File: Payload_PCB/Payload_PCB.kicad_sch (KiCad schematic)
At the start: 22 parts, among them J2 Conn_01x03, J3 Conn_01x03, J4 Conn_01x03, Q4 PMOS, Q5 PMOS, Q6 NMOS, U1 TSR_1-2450

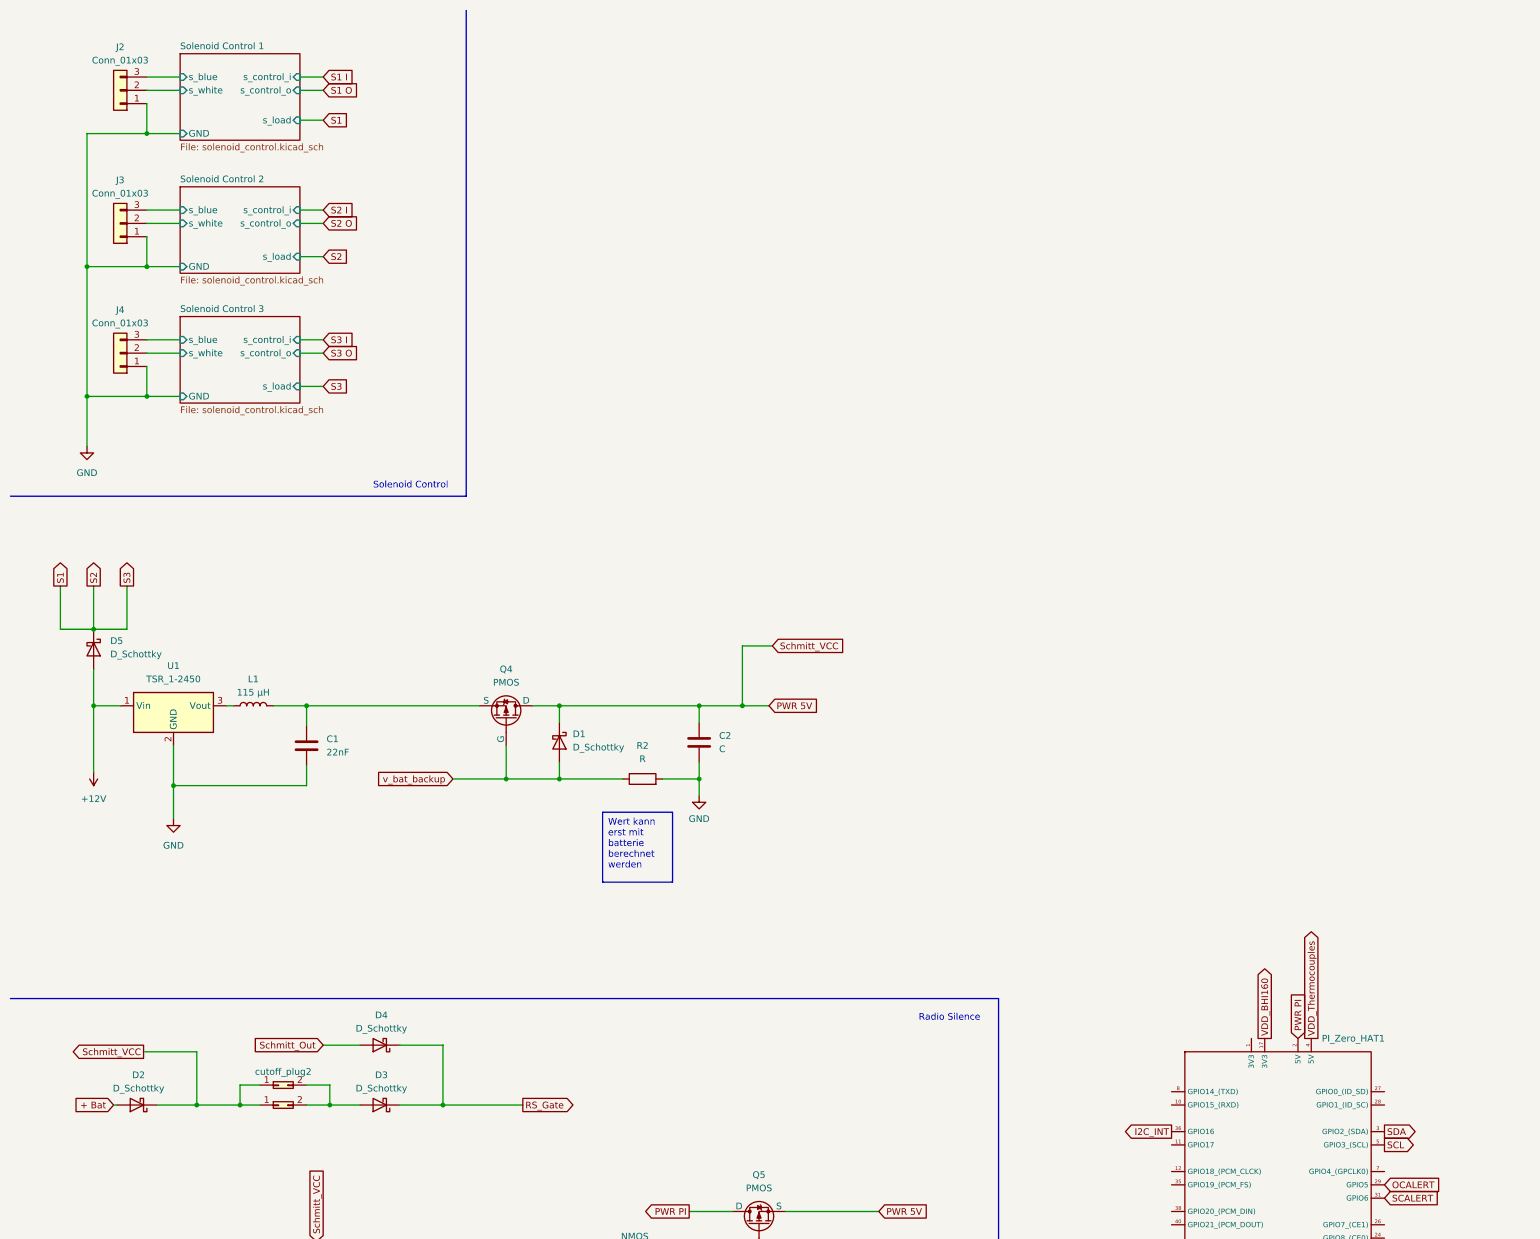
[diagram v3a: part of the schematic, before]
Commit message: Added bms chip (not yet connected to power)
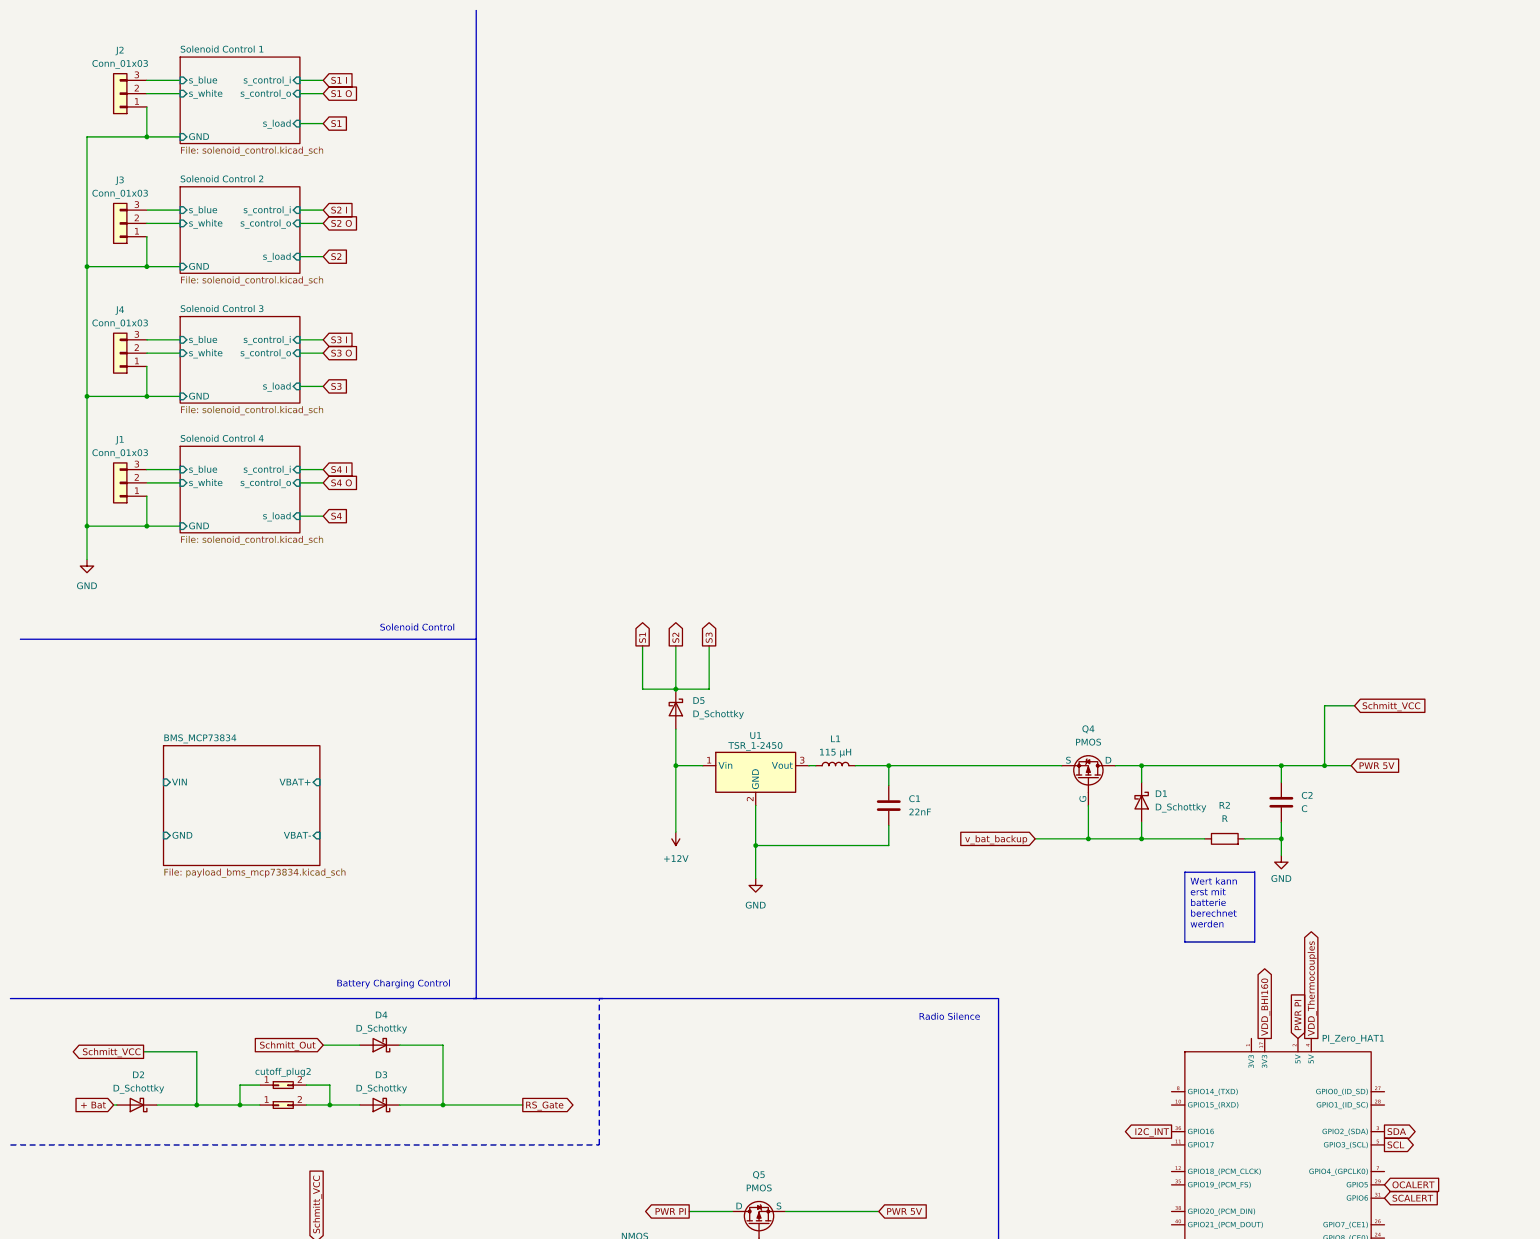
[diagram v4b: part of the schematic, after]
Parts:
- added J1: Conn_01x03, symbol Connector_Generic:Conn_01x03
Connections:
- net GND: now also J1.1 (Pin_1)
- new net Solenoid Control 4/s_blue: J1.3 (Pin_3)
- new net Solenoid Control 4/s_white: J1.2 (Pin_2)
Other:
- added sheet BMS_MCP73834 (payload_bms_mcp73834.kicad_sch)
- added sheet Solenoid Control 4 (solenoid_control.kicad_sch)
- note added: "Battery Charging Control"
- moved on the sheet: C1, C2, D1, D5, J2, L1, Q4, R2, U1

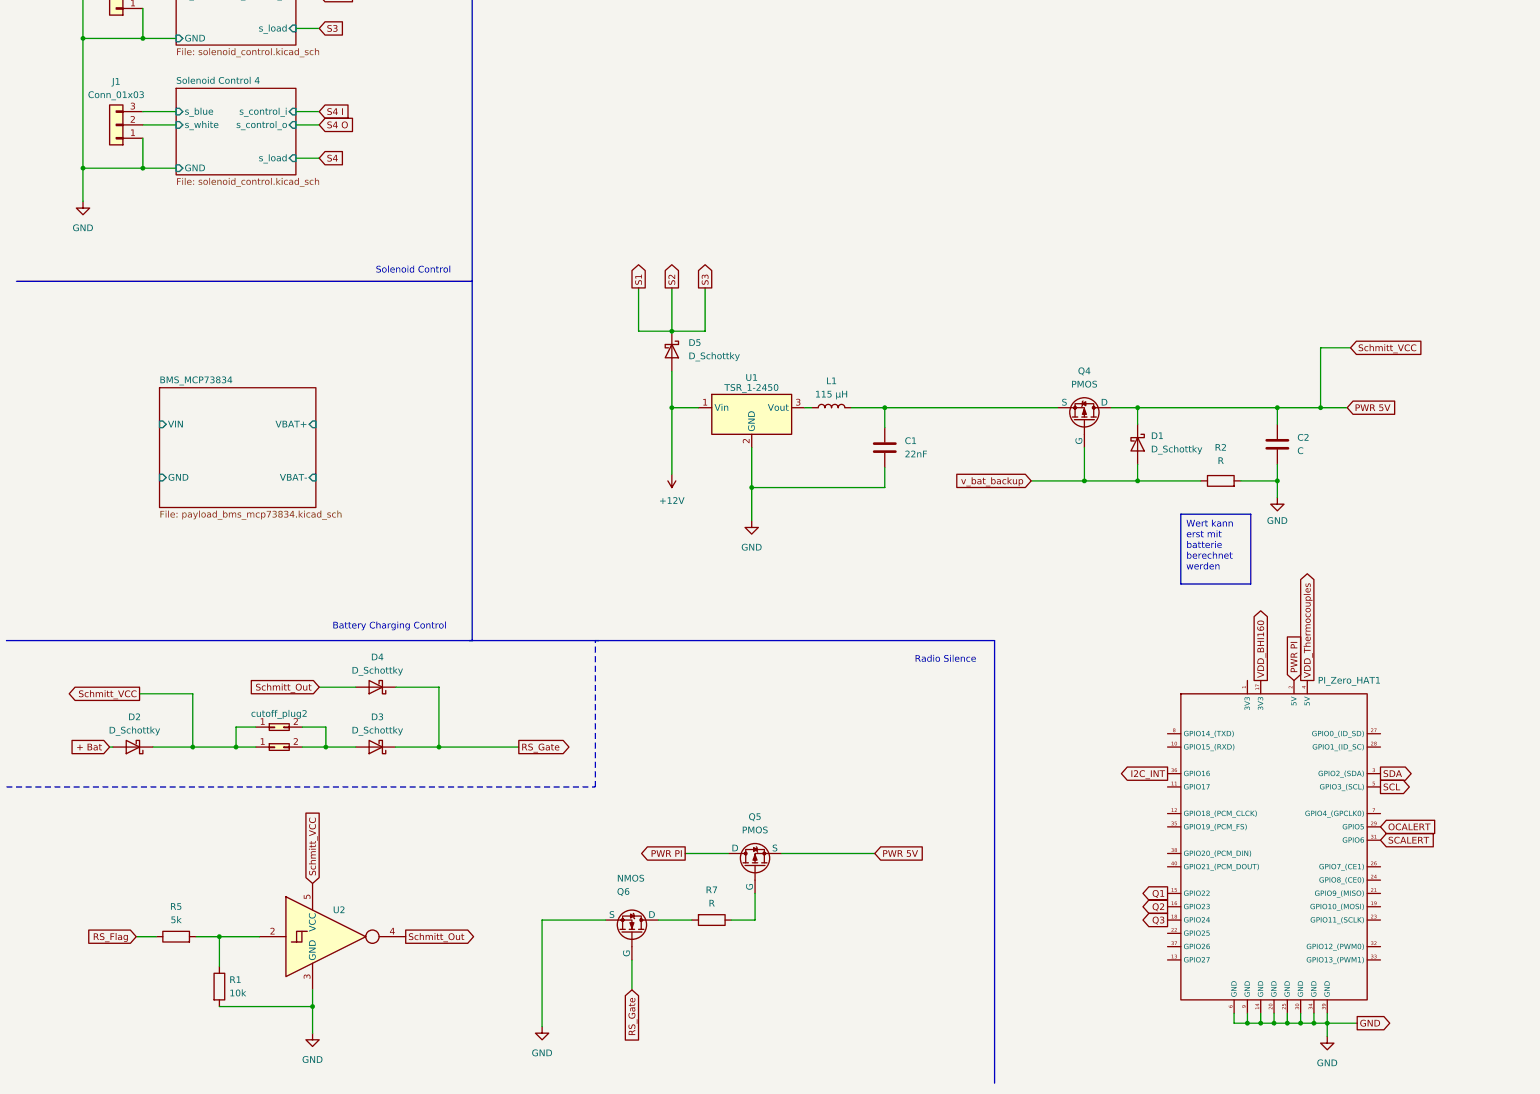
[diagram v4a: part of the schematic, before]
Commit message: Added Payload Harness Connector
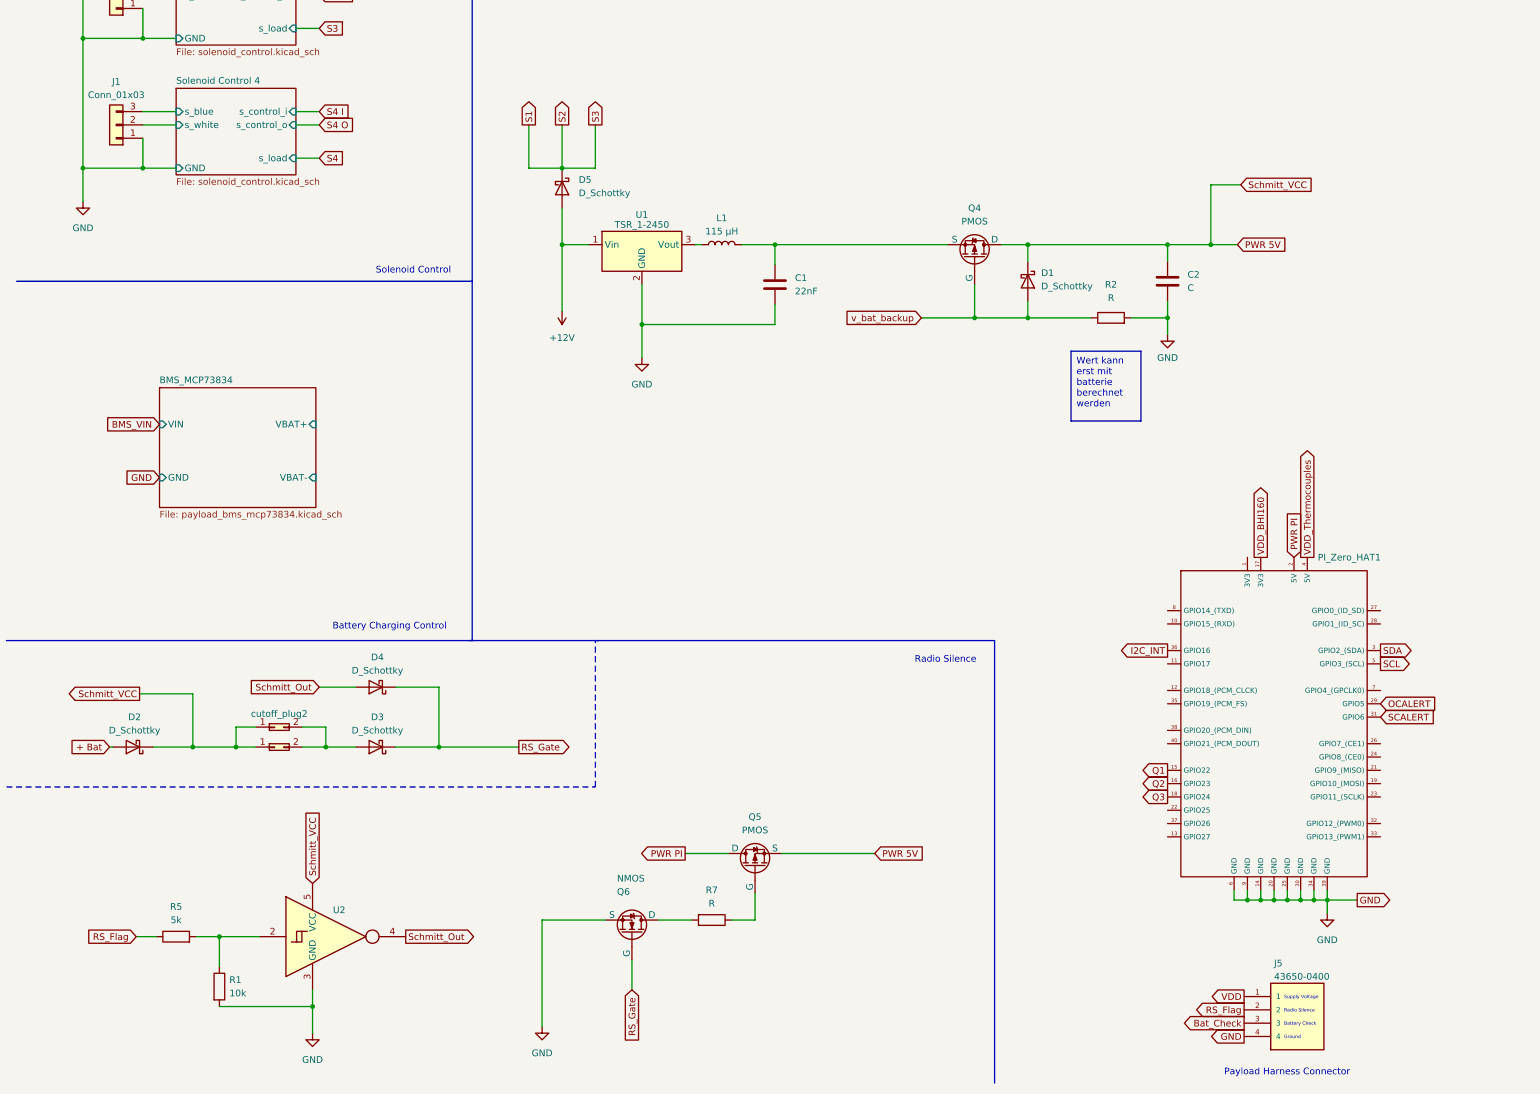
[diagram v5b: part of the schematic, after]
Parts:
- added J5: 43650-0400, 43650-0400:MOLEX_43650-0400, symbol 43650-0400:43650-0400
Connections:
- net GND: now also J5.4
- net RS_Flag: now also J5.2
- new net Bat_Check: J5.3
- new net VDD: J5.1
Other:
- note added: "Battery Check"
- note added: "Ground"
- note added: "Payload Harness Connector"
- note added: "Supply Voltage"
- moved on the sheet: C1, C2, D1, D5, L1, PI_Zero_HAT1, Q4, R2, U1

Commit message: Minor changes and corrections
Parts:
- added C18: 22nF, symbol Device:C
- added L2: 115 µH, symbol Device:L
- added U10: TSR_1-2450, Converter_DCDC:Converter_DCDC_TRACO_TSR-1_THT, symbol Regulator_Switching:TSR_1-2450
- renumbered D2 to D1, D4 to D2, D5 to D4, D1 to D5, J2 to J1, J3 to J2, J4 to J3, J1 to J4, Q6 to Q1, Q5 to Q2, Q4 to Q3, R5 to R1, R1 to R2, R7 to R3, R2 to R4, U2 to U1, U1 to U2, cutoff_plug2 to cutoff_plug1
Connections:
- net Q1 is gone; now on net S1 I: PI_Zero_HAT1.15 (GPIO22)
- net Q2 is gone; now on net S1 O: PI_Zero_HAT1.16 (GPIO23)
- net Q3 is gone; now on net S2 I: PI_Zero_HAT1.18 (GPIO24)
- net GND: now also C18.2, U10.2 (GND)
- net I2C_INT: now also PI_Zero_HAT1.8 (GPIO14_(TXD)); no longer PI_Zero_HAT1.36 (GPIO16)
- net S2 O: now also PI_Zero_HAT1.22 (GPIO25)
- net S3 I: now also PI_Zero_HAT1.37 (GPIO26)
- net S3 O: now also PI_Zero_HAT1.13 (GPIO27)
- net S4 I: now also PI_Zero_HAT1.36 (GPIO16)
- net S4 O: now also PI_Zero_HAT1.11 (GPIO17)
- net +12V renamed S_LOAD
- net S_LOAD: no longer U2.1 (Vin)
- net v_bat_backup: no longer names the net of D5.2 (A), Q3.2 (G), R4.1
- net v_bat_backup: now also C18.1, L2.2
- new net: L2.1, U10.3 (Vout)
- new net VBAT+: U2.1 (Vin)
- new net VBAT+_Backup: U10.1 (Vin)
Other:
- added sheet BMS_MCP73835 (payload_bms_mcp73834.kicad_sch)
- sheet BMS_MCP73834 ports: added none; removed VBAT-
- moved on the sheet: C1, D4, L1, U2

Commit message: Added BMI088 and BMP390
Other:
- note added: "backup_bat"
- note added: "main_bat"
- note added: "Änderung zu boost convertern nötig"
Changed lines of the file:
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@@
     (effects (font (size 1.27 1.27)) (justify left top))
+  )
+  (text "Änderung zu boost convertern nötig\n" (at 125.73 113.665 0)
+    (effects (font (size 1.27 1.27)) (justify left bottom))
   )
   (text "TODO: Maybe only one VDD and distribute among sensors?\n"
@@
     (effects (font (size 0.635 0.635)) (justify left bottom))
   )
+  (text "backup_bat\n" (at 43.815 165.1 0)
+    (effects (font (size 1.27 1.27)) (justify left bottom))
+  )
   (text "Radio Silence" (at 255.905 271.78 0)
     (effects (font (size 0.635 0.635)) (justify left bottom))
   )
-  (text "Battery Charging Control\n" (at 74.295 198.755 0)
+  (text "Battery Charging Control\n" (at 80.645 198.755 0)
     (effects (font (size 1.27 1.27)) (justify left bottom))
   )
@@
     (effects (font (size 1.27 1.27)) (justify left bottom))
   )
+  (text "main_bat" (at 43.815 137.795 0)
+    (effects (font (size 1.27 1.27)) (justify left bottom))
+  )
   (text "Solenoid Control" (at 82.55 130.81 0)
     (effects (font (size 1.27 1.27)) (justify left bottom))
@@
     )
   )
-  (global_label "GND" (shape input) (at 44.45 182.88 180) (fields_autoplaced)
-    (effects (font (size 1.27 1.27)) (justify right))
-    (property "Intersheetrefs" "${INTERSHEET_REFS}" (at 37.5943 182.88 0)
+  (global_label "GND" (shape input) (at 43.815 182.88 180) (fields_autoplaced)
+    (effects (font (size 1.27 1.27)) (justify right))
+    (property "Intersheetrefs" "${INTERSHEET_REFS}" (at 36.9593 182.88 0)
       (effects (font (size 1.27 1.27)) (justify right) hide)
     )
@@
     )
   )
-  (global_label "VBAT+_Backup" (shape output) (at 61.595 177.165 0) (fields_autoplaced)
-    (effects (font (size 1.27 1.27)) (justify left))
-    (property "Intersheetrefs" "${INTERSHEET_REFS}" (at 78.3687 177.165 0)
+  (global_label "VBAT+_Backup" (shape output) (at 60.96 177.165 0) (fields_autoplaced)
+    (effects (font (size 1.27 1.27)) (justify left))
+    (property "Intersheetrefs" "${INTERSHEET_REFS}" (at 77.7337 177.165 0)
       (effects (font (size 1.27 1.27)) (justify left) hide)
     )
@@
     )
   )
-  (global_label "BMS_VIN" (shape input) (at 44.45 172.72 180) (fields_autoplaced)
-    (effects (font (size 1.27 1.27)) (justify right))
-    (property "Intersheetrefs" "${INTERSHEET_REFS}" (at 33.5424 172.72 0)
+  (global_label "BMS_VIN" (shape input) (at 43.815 172.72 180) (fields_autoplaced)
+    (effects (font (size 1.27 1.27)) (justify right))
+    (property "Intersheetrefs" "${INTERSHEET_REFS}" (at 32.9074 172.72 0)
       (effects (font (size 1.27 1.27)) (justify right) hide)
     )
@@
     )
   )
-  (sheet (at 44.45 168.275) (size 17.145 17.78) (fields_autoplaced)
+  (sheet (at 43.815 168.275) (size 17.145 17.78) (fields_autoplaced)
     (stroke (width 0.1524) (type solid))
     (fill (color 0 0 0 0.0000))
-    (property "Sheetname" "BMS_MCP73835" (at 44.45 167.5634 0)
+    (property "Sheetname" "BMS_MCP73835" (at 43.815 167.5634 0)
       (effects (font (size 1.27 1.27)) (justify left bottom))
     )
-    (property "Sheetfile" "payload_bms_mcp73834.kicad_sch" (at 44.45 186.6396 0)
+    (property "Sheetfile" "payload_bms_mcp73834.kicad_sch" (at 43.815 186.6396 0)
       (effects (font (size 1.27 1.27)) (justify left top))
     )
-    (pin "GND" input (at 44.45 182.88 180)
-      (effects (font (size 1.27 1.27)) (justify left))
-    )
-    (pin "VIN" input (at 44.45 172.72 180)
-      (effects (font (size 1.27 1.27)) (justify left))
-    )
-    (pin "VBAT+" input (at 61.595 177.165 0)
+    (pin "GND" input (at 43.815 182.88 180)
+      (effects (font (size 1.27 1.27)) (justify left))
+    )
+    (pin "VIN" input (at 43.815 172.72 180)
+      (effects (font (size 1.27 1.27)) (justify left))
+    )
+    (pin "VBAT+" input (at 60.96 177.165 0)
       (effects (font (size 1.27 1.27)) (justify right))
     )

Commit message: Added supply voltage for sensors and changed Radio Silence location
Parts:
- removed Q1: NMOS, symbol Simulation_SPICE:NMOS
- added C21: 0.1uF, symbol Device:C
- added Q1, Q12: PMOS, symbol Simulation_SPICE:PMOS
- added R47: 10 Ohm, symbol Device:R
- R3: value R -> 10kOhm
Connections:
- net + Bat is gone; now on net VDD: D1.2 (A)
- net BMS_VIN: now also Q2.1 (D)
- net PWR 5V: no longer Q2.3 (S)
- net PWR PI: no longer Q2.1 (D)
- net RS_Gate: now also Q1.2 (G)
- net VDD: now also Q1.3 (S), Q12.1 (D)
- net at R3.2: now also Q2.3 (S), C21.1, Q12.3 (S)
- net at Q2.2 (G), R3.1: now also C21.2, Q12.2 (G), R47.2
- net VDD_BHI160 renamed VDD_S_Main
- new net: Q1.1 (D), R47.1
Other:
- sheet Sensor Modules ports: added VDD_S; removed VDD_BHI160
- moved on the sheet: Q2
